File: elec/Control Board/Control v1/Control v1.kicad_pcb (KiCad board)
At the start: 2 copper layers, 126.3 x 160 mm, 212 parts, among them J1 DB9_Female_MountingHoles, J10 Conn_02x12_Odd_Even, J11 Screw_Terminal_01x02, J12 Screw_Terminal_01x02, J13 Screw_Terminal_01x02, J14 Conn_01x10, J15 DB25_Female_MountingHoles, J16 Conn_01x04, J17 Conn_01x05, J18 Conn_01x04, J19 Conn_01x07, J2 Conn_01x08, J20 Conn_01x04, J21 RJ12_6P6C_HORZ, J22 0.100_2Pin, J23 0.100_2Pin, J24 Conn_01x04, J25 Screw_Terminal_01x02, J3 Conn_01x08, J4 Conn_01x08, J5 Conn_01x08, J6 Conn_01x08, J7 Conn_01x10, J8 Conn_02x18_Odd_Even, J9 Conn_01x10, Q1 BSS138, Q10 BSS138, Q2 NCE01P30K, Q3 BSS138, Q4 BSS138, Q5 BSS138, Q6 BSS138, Q7 BSS138, Q8 BSS138, Q9 BSS138

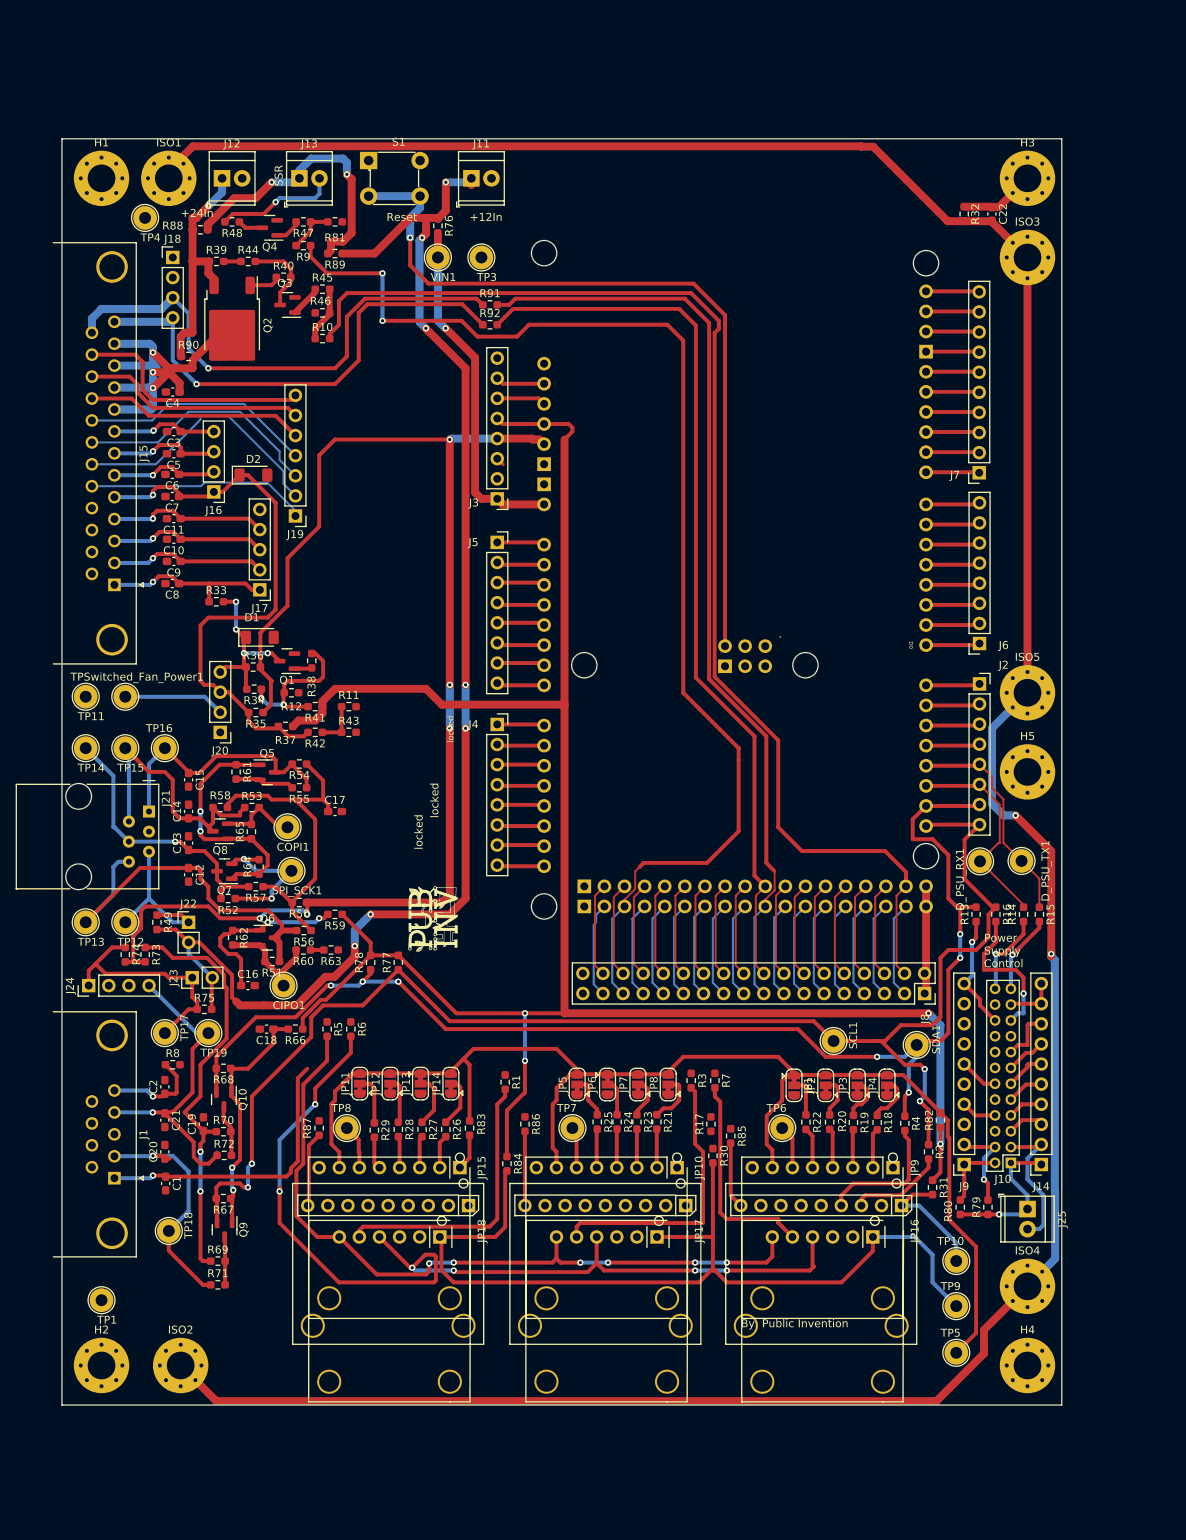
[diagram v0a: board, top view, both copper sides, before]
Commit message: Enlarge perimeter. Resume routing.
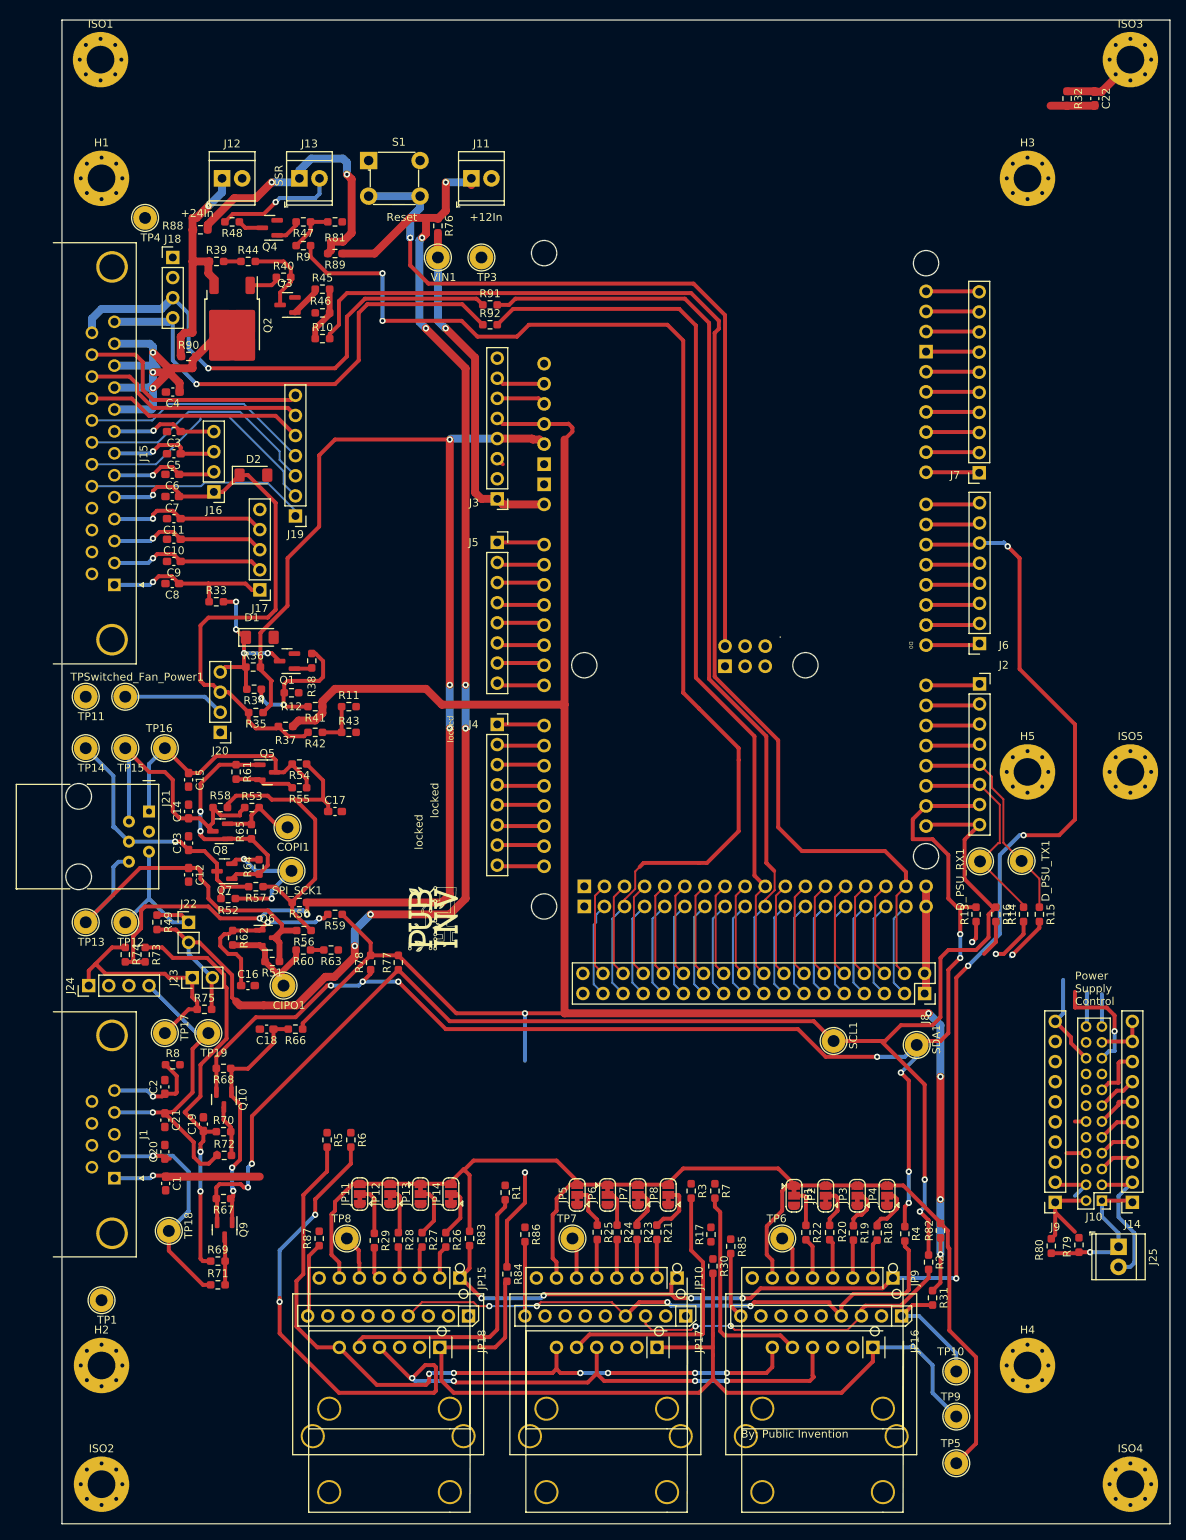
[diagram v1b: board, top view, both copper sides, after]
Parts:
- moved ISO3 28.2 mm to (185.0, 40.0)
- moved ISO4 28.2 mm to (185.0, 220.0)
- moved C22 19.5 mm to (180.5, 44.9)
- moved R32 19.5 mm to (177.0, 44.9)
- moved ISO2 18.0 mm to (55.0, 220.0)
- moved ISO1 17.3 mm to (54.9, 40.0)
- moved ISO5 16.4 mm to (185.0, 130.0)
- moved R5 14.0 mm to (83.5, 176.5)
- moved R6 14.0 mm to (86.5, 176.5)
- moved JP1 14.0 mm to (142.5, 183.6)
- moved JP2 14.0 mm to (146.5, 183.6)
- moved JP3 14.0 mm to (150.5, 183.6)
- moved JP4 14.0 mm to (154.2, 183.6)
- moved R1 14.0 mm to (106.0, 183.2)
- moved R21 14.0 mm to (125.2, 188.2)
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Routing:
- net Net-(C22-Pad2): track 371.6 -> 5.61 mm, vias 2 -> 0
- net ONE_WIRE_TC: track 11.4 -> 188.0 mm, vias 0 -> 8
- net /Thermocouple Amplifier I2C breakout board - MCP9600/SDA: track 17.0 -> 75.7 mm, vias 0 -> 4
- net /Thermocouple Amplifier I2C breakout board - MCP9600/SCL: track 12.0 -> 41.8 mm, vias 0 -> 2
- net D39: track 48.9 -> 30.8 mm
- net SDA: track 160.6 -> 175.4 mm, vias 7 -> 9
- net +3.3V: track 259.1 -> 272.7 mm, vias 4 -> 6
- net SCL: track 177.5 -> 187.3 mm
- net /VO-: track 11.5 -> 5.55 mm, vias 1 -> 0
- net /VO+: track 8.67 -> 12.2 mm
- net /AUX: track 11.4 -> 7.93 mm
- net /VSET: track 4.48 -> 2.49 mm
- net /Thermocouple Amplifier SPI Interface breakout board - MAX31855 /nCS_2: track 35.2 -> 34.4 mm
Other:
- board size 126.3 x 160 mm -> 140 x 190 mm

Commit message: Finishe routing on enlarged perimeter.
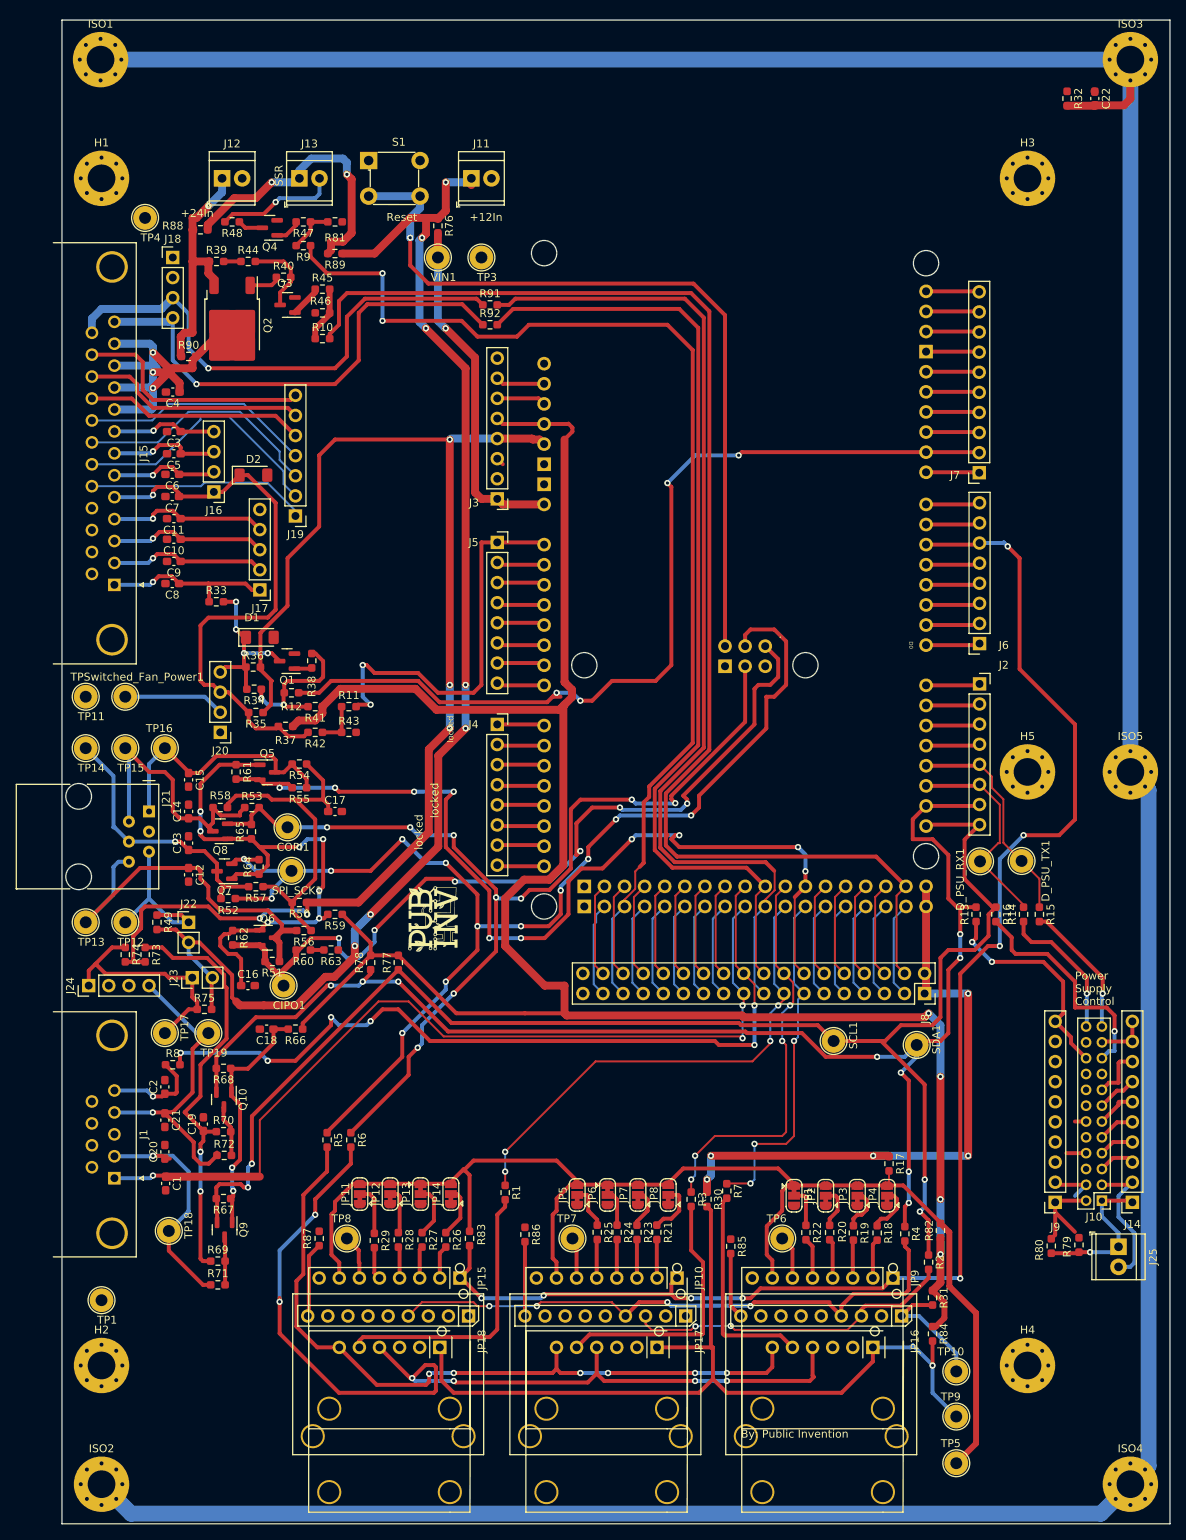
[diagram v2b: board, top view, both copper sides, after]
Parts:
- moved R84 54.3 mm to (160.0, 201.0)
- moved R17 24.2 mm to (154.5, 179.5), turned to -90 degrees
- moved R30 8.48 mm to (131.5, 184.0)
- moved R7 1.50 mm to (134.0, 182.9)
- moved R3 1.05 mm to (129.5, 184.0)
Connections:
- A1 pad 5V2: +5V -> unconnected-(A1-SPI_5V-Pad5V2)
- A1 pad 5V3: +5V -> 5VHead
- A1 pad 5V4: +5V -> 5VHead
- J8 pad 1: +5V -> 5VHead
- J8 pad 2: +5V -> 5VHead
- R17 pad 1: +5V -> 5VHead
- R30 pad 1: +5V -> 5VHead
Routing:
- net Net-(C22-Pad2): track 5.61 -> 458.4 mm
- net SPI_SCK: track 19.4 -> 156.2 mm, vias 2 -> 13
- net COPI: track 10.2 -> 132.9 mm, vias 0 -> 9
- net nFAN1_PWM: track 6.75 -> 116.9 mm, vias 0 -> 4
- net D32: track 19.6 -> 118.4 mm, vias 0 -> 10
- net CIPO: track 14.9 -> 106.7 mm, vias 0 -> 6
- net D38: track 11.9 -> 101.9 mm, vias 0 -> 6
- net D39: track 30.8 -> 112.8 mm, vias 1 -> 3
- net 5VHead: track 0.00 -> 78.9 mm, vias 0 -> 5
- net TC_nCS3: track 12.1 -> 62.5 mm, vias 0 -> 4
- net BLOWER_TACH: track 6.04 -> 50.3 mm, vias 0 -> 2
- net TC_nCS2: track 11.9 -> 50.8 mm, vias 0 -> 4
- net TC_nCS1: track 12.1 -> 44.3 mm, vias 0 -> 3
- net +5V: track 189.2 -> 169.4 mm
- net /SPI_ControllerLevel_Shifter/+3V3Local: track 53.6 -> 72.3 mm, vias 4 -> 7
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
